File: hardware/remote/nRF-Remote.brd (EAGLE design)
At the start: 77 x 30.2 mm, 26 parts, among them IC1 TP4056, IC2 TPS769XX, J1 62000611121, J2 61300211121, M1 WIRELESS-NRF24L01, SW1 B3F-1000, U1 ATMEGA328P-AU

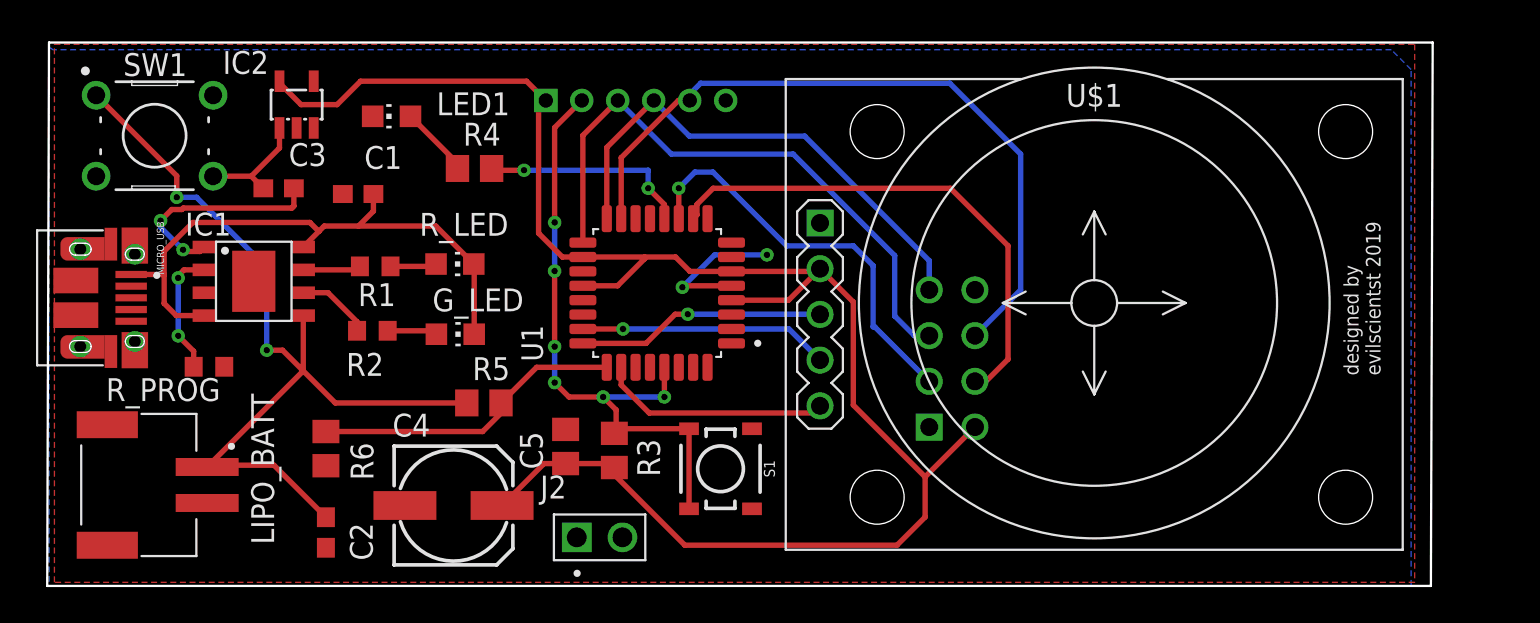
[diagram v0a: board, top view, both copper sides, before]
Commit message: Update design with external XTAL, add buttons
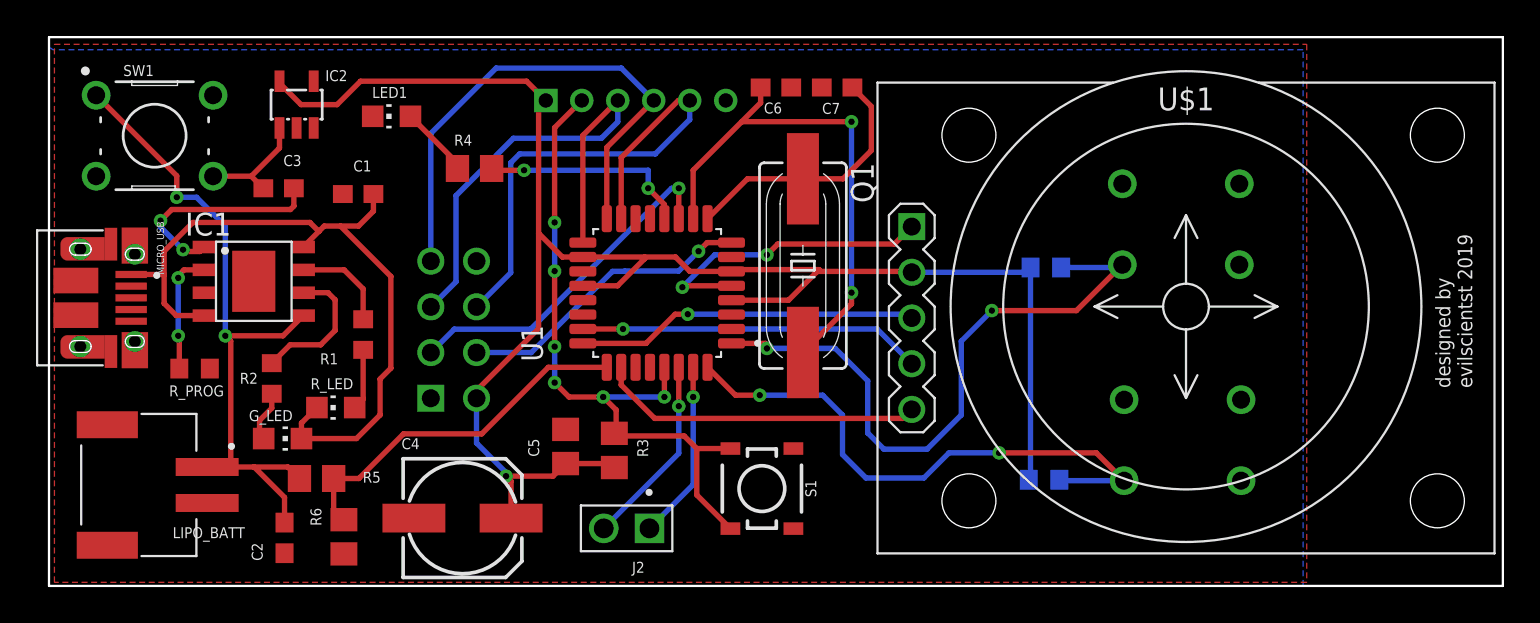
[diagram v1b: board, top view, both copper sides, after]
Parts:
- added C6, C7: 20pF, rcl:C0603
- added Q1: 16MHz, adafruit:SM49
- added R7, R8: 10K, rcl:R0603
- added SW2, SW3: B3F-1000, Switch:B3F-1000
- moved M1 27.7 mm to (33.9, 16.8)
- moved G_LED 11.2 mm to (13.0, 8.19)
- moved R_LED 10.4 mm to (15.9, 9.91), turned to 90 degrees
- moved R5 10.2 mm to (14.9, 5.97)
- moved R2 6.19 mm to (12.4, 11.5), turned to 90 degrees
- moved U$1 5.10 mm to (63.2, 14.9)
- moved R6 5.00 mm to (16.4, 2.73)
- moved R1 3.85 mm to (17.5, 14.0), turned to 90 degrees
- moved S1 2.55 mm to (39.6, 5.41)
- moved C2 2.32 mm to (13.1, 2.67)
- moved J2 1.58 mm to (32.1, 3.20), turned to 180 degrees
- moved C4 0.86 mm to (23.0, 3.77)
- moved R_PROG 0.81 mm to (8.09, 12.1)
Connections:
- net RX renamed N$15
- net TX renamed N$16
- new net N$10: C7.2, Q1.1, U1.9
- new net N$8: C6.2, Q1.2, U1.10
- new net SW1: R7.1, SW2.1, U1.1
- new net SW2: R8.1, SW3.1, U1.32
- net +3V3: now also R7.2, R8.2
- net CSN: now also U1.8; no longer U1.10
- net GND: now also C6.1, C7.1, SW2.4, SW3.4
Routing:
- net SW1: track 0.00 -> 36.1 mm, vias 0 -> 2
- net SW2: track 0.00 -> 31.8 mm, vias 0 -> 2
- net N$8: track 0.00 -> 28.9 mm, vias 0 -> 2
- net N$10: track 0.00 -> 14.6 mm
- net CSN: track 28.5 -> 16.7 mm, vias 0 -> 1
- net MOSI: track 40.3 -> 29.3 mm
- net V_BATT: track 49.4 -> 38.5 mm
- net N$15: track 0.00 -> 10.7 mm, vias 0 -> 1
- net N$16: track 0.00 -> 9.96 mm, vias 0 -> 1
- net GND: track 20.4 -> 29.1 mm
- net +5V: track 33.6 -> 41.3 mm
- net SCK: track 33.4 -> 27.3 mm
- net JS_SW: track 12.8 -> 18.1 mm
- net ADC_1: track 13.9 -> 19.0 mm
- net ADC_0: track 13.9 -> 19.1 mm
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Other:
- board size 77 x 30.2 mm -> 80.8 x 30.5 mm
